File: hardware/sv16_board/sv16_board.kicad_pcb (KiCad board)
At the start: 4 copper layers, 122 x 122 mm, 141 parts, among them J1 JTAG, J10 CONSOLE, J2 JTAG-1.27, J3 EXP-A, J4 EXP-B, J5 EXP-C, J6 MOTOR, J7 SPARE (not fitted), J8 USB-C, J9 7-12 V, Q1 2N7002, Q2 BC817, Q4 BC807, SW1 RESET, SW2 RECONFIG, U1 LFE5U-12F-6TG144C, U2 W25Q64JVSSIQ, U3 W25Q64JVSSIQ, U4 CH340G, U5 AP62300TWU-7, U6 MP1584EN, U7 LP5907MFX-2.5, U8 USBLC6-2SC6, Y1 25 MHz ACTIVE XO (4-pin), Y2 12 MHz (CH340G clock)

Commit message: Add the KiCad schematic, and fix the two bugs it exposed
The sheet is generated from the same netlist the board is built from
(CONNECTIONS is (ref, pad, net)), so the two views cannot drift: --check fails
if a net or a pad is on one and not the other.  132 symbols, 472 labelled pins,
118 nets, one A0 sheet.  Symbols are built from each part's own pad list, so
the USB-C connector shows A1..B12 and S1..S4 instead of being flattened into
1..20.  Mounting holes, fiducials and the unfitted spare header are left off:
they carry no nets and a pad with no number is not a pin.

Generating it turned up two real faults.

Three pads were each on two nets.  U1 pins 46, 47 and 49 are the ECP5's
configuration pins (MISO, MOSI, CSSPIN) and double as gpio_a[1], gpio_a[2] and
gpio_a[4] once the device has booted - sv16_board_pins.py marks all three dual
purpose and the .lpf locates gpio_a[1..4] there.  The netlist named the same
copper twice, and since a pad can only hold one net, three connections were
being dropped silently on both the board and the sheet.  They are one net now,
named for the GPIO they become so the sheet reads like the HDL, with the flash
hanging on the same copper through R10/R11/R12.

JP1 had been left sitting on top of J7 by a half-finished edit of its own
placement (a literal 'if False else'), overlapping four pads by up to 0.7 mm.
It is back at the position that was clear.  Placement now reports no
violations.

The board file is regenerated from the corrected netlist, so it is placement
only again - the previous routing referenced the old nets and has to be re-run.

Co-authored-by: arena-agent <297053741+arena-agent@users.noreply.github.com>
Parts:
- moved JP1 11.9 mm to (26.0, 82.5)
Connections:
- R10 pad 1: MOSI -> A2
- R11 pad 1: MISO -> A1
- R12 pad 1: CSSPIN -> A4
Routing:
- net U6_SW: track 255.8 -> 0.00 mm, vias 35 -> 0
- net U2_DO: track 147.3 -> 0.00 mm, vias 78 -> 0
- net VM_IN: track 135.8 -> 0.00 mm, vias 8 -> 0
- net USB_VBUS: track 113.2 -> 0.00 mm, vias 6 -> 0
- net U4_DTR: track 105.7 -> 0.00 mm, vias 1 -> 0
- net U2_CLK: track 82.7 -> 0.00 mm, vias 7 -> 0
- net uart_rx: track 71.0 -> 0.00 mm, vias 1 -> 0
- net U2_DI: track 68.2 -> 0.00 mm, vias 8 -> 0
- net A5: track 67.8 -> 0.00 mm, vias 4 -> 0
- net A4: track 67.0 -> 0.00 mm, vias 1 -> 0
- net GND: track 64.0 -> 0.00 mm, vias 87 -> 0
- net A6: track 63.3 -> 0.00 mm, vias 3 -> 0
- net clk_25m: track 62.7 -> 0.00 mm, vias 7 -> 0
- net PROGRAMN: track 61.6 -> 0.00 mm, vias 5 -> 0
- net INITN: track 61.5 -> 0.00 mm, vias 7 -> 0
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- removed copper zone on In2.Cu, net 1V1
- removed copper zone on In2.Cu, net 2V5
- removed copper zone on In2.Cu, net 3V3
- removed copper zone on In2.Cu, net USB_VBUS
- removed copper zone on In2.Cu, net VM_IN
- removed copper zone on In2.Cu, net VM_IN_RAW

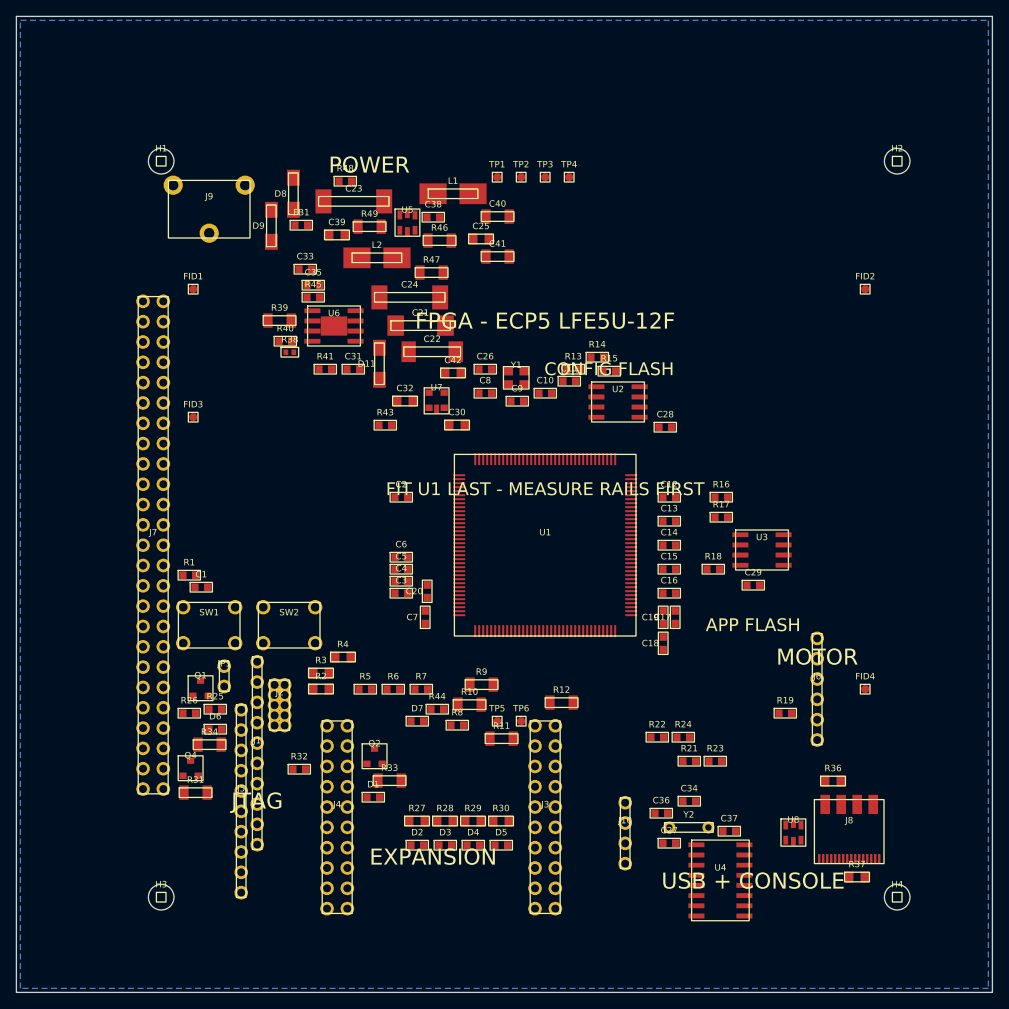
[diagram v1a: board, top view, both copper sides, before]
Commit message: Rename the LED nets off KiCad's bus notation
led[0]_k and its siblings use square brackets, which KiCad reads as
bus-vector syntax: a label of led[2]_k is not a name it can parse, and
the sheet was rejected on load.  They are now led0_k, led1_k and so on,
renamed at source so the board and the sheet stay in step.

The generator now refuses any net name containing brackets, whitespace
or other characters KiCad reserves.

Co-authored-by: arena-agent <297053741+arena-agent@users.noreply.github.com>
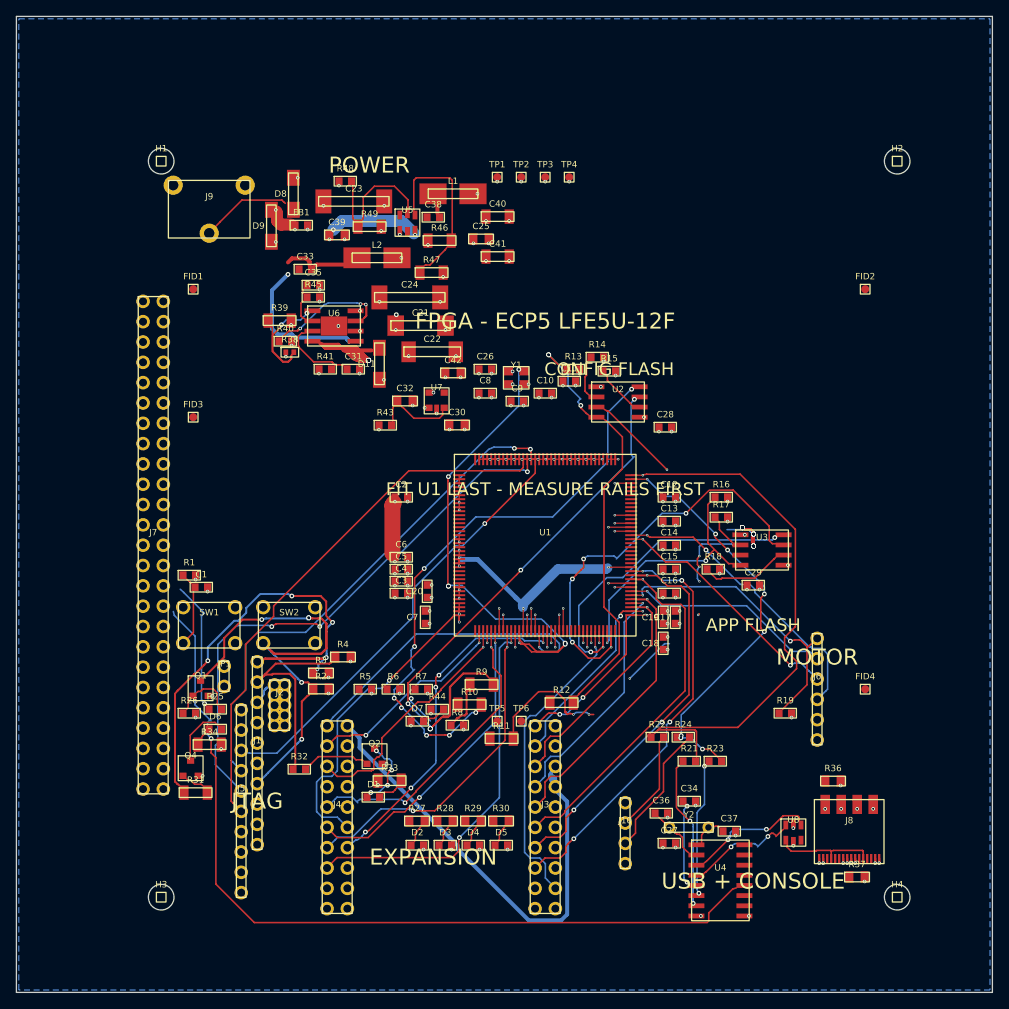
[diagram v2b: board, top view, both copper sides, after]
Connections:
- net led[0] renamed led0
- net led[0]_k renamed led0_k
- net led[1] renamed led1
- net led[1]_k renamed led1_k
- net led[2] renamed led2
- net led[2]_k renamed led2_k
- net led[3] renamed led3
- net led[3]_k renamed led3_k
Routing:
- net U6_FREQ: track 0.00 -> 255.8 mm, vias 0 -> 35
- net U2_WP: track 0.00 -> 147.3 mm, vias 0 -> 78
- net VM_IN: track 0.00 -> 135.8 mm, vias 0 -> 8
- net USB_DP_F: track 0.00 -> 113.2 mm, vias 0 -> 6
- net Y2_XO: track 0.00 -> 105.7 mm, vias 0 -> 1
- net U2_CLK: track 0.00 -> 82.7 mm, vias 0 -> 7
- net U4_RXD: track 0.00 -> 71.0 mm, vias 0 -> 1
- net U2_DO: track 0.00 -> 68.2 mm, vias 0 -> 8
- net A8: track 0.00 -> 67.8 mm, vias 0 -> 4
- net A7: track 0.00 -> 67.0 mm, vias 0 -> 1
- net GND: track 0.00 -> 64.0 mm, vias 0 -> 87
- net A9: track 0.00 -> 63.3 mm, vias 0 -> 3
- net U4_TXD: track 0.00 -> 62.7 mm, vias 0 -> 7
- net CFG_0: track 0.00 -> 61.6 mm, vias 0 -> 5
- net CFG_1: track 0.00 -> 61.5 mm, vias 0 -> 7
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- added copper zone on In2.Cu, net 1V1
- added copper zone on In2.Cu, net 2V5
- added copper zone on In2.Cu, net 3V3
- added copper zone on In2.Cu, net USB_VBUS
- added copper zone on In2.Cu, net VM_IN
- added copper zone on In2.Cu, net VM_IN_RAW
